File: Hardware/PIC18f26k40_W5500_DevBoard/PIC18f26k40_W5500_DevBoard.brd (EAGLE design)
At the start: 58 x 57 mm, 41 parts, among them J2 MAGJACK, U1 W5500, U2 PIC18F2523-I/SO

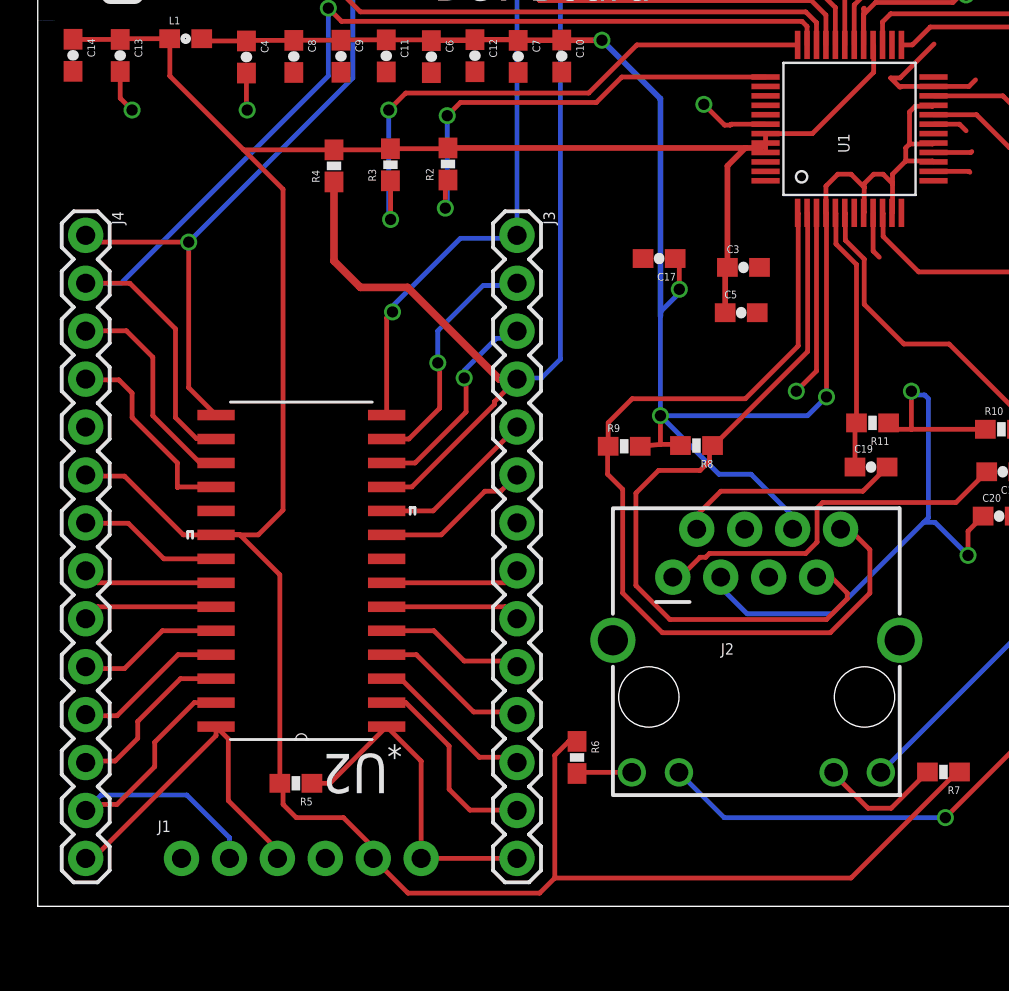
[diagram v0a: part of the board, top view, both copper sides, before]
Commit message: #251 Added more labeling to board
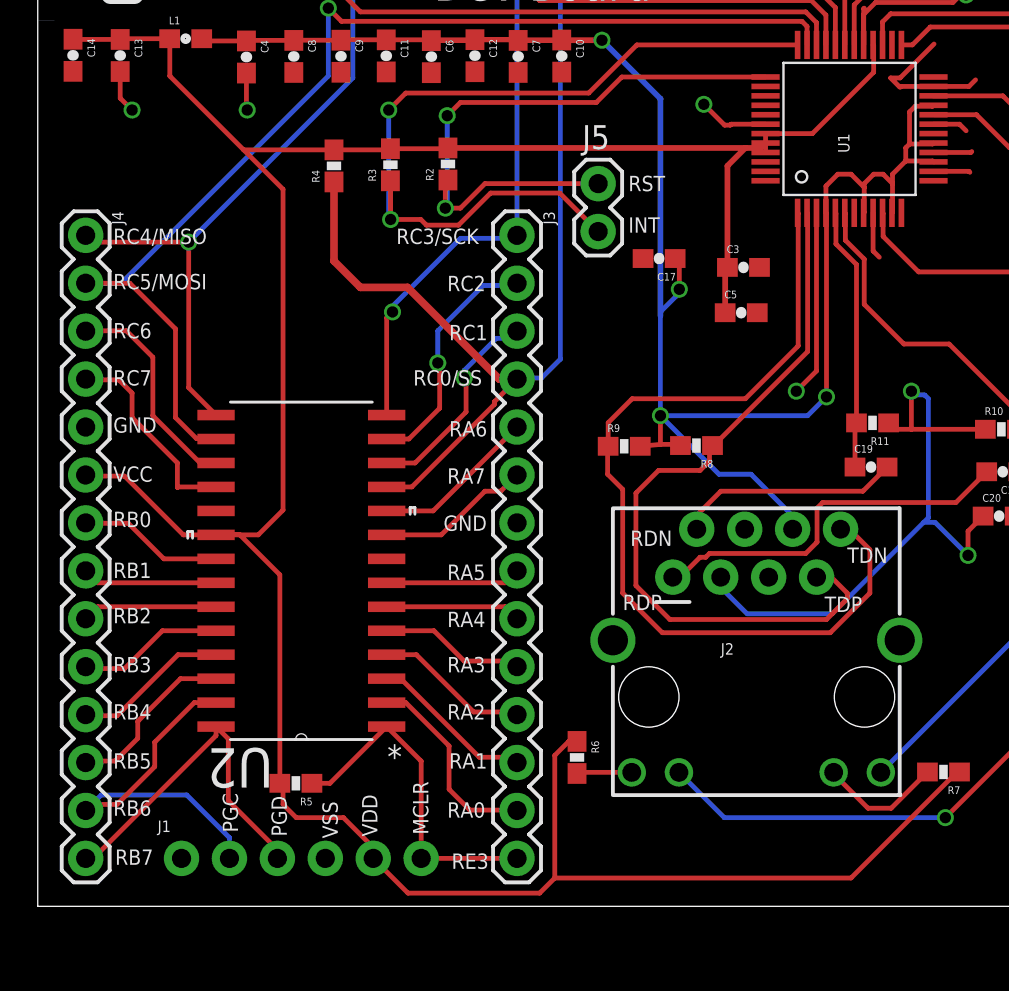
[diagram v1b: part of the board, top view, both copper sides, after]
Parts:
- added J5: (no value), SparkFun-Connectors:1X02
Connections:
- net INT: now also J5.2
- net RST: now also J5.1
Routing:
- net INT: track 31.0 -> 43.7 mm
- net RST: track 24.2 -> 32.8 mm
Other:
- board text added: "GND"
- board text added: "INT"
- board text added: "MCLR"
- board text added: "PGC"
- board text added: "PGD"
- board text added: "RA0"
- board text added: "RA1"
- board text added: "RA2"
- board text added: "RA3"
- board text added: "RA4"
- board text added: "RA5"
- board text added: "RA6"
- board text added: "RA7"
- board text added: "RB0"
- board text added: "RB1"
- board text added: "RB2"
- board text added: "RB3"
- board text added: "RB4"
- board text added: "RB5"
- board text added: "RB6"
- board text added: "RB7"
- board text added: "RC0/SS"
- board text added: "RC1"
- board text added: "RC2"
- board text added: "RC3/SCK"
- board text added: "RC4/MISO"
- board text added: "RC5/MOSI"
- board text added: "RC6"
- board text added: "RC7"
- board text added: "RDN"
- board text added: "RDP"
- board text added: "RE3"
- board text added: "RST"
- board text added: "TDN"
- board text added: "TDP"
- board text added: "VCC"
- board text added: "VDD"
- board text added: "VSS"
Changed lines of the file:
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@@
 <text x="21" y="51" size="1.778" layer="21">W5500</text>
 <text x="21" y="48" size="1.778" layer="21">Dev Board</text>
+<text x="9.8" y="6" size="0.8128" layer="21" rot="R270">PGC</text>
+<text x="13.2" y="3.7" size="0.8128" layer="21" rot="R90">PGD</text>
+<text x="15.9" y="3.6" size="0.8128" layer="21" rot="R90">VSS</text>
+<text x="18" y="3.7" size="0.8128" layer="21" rot="R90">VDD</text>
+<text x="20.7" y="3.8" size="0.8128" layer="21" rot="R90">MCLR</text>
+<text x="23.9" y="2.8" size="0.8128" layer="21" rot="R180">RE3</text>
+<text x="21.7" y="4.7" size="0.8128" layer="21">RA0</text>
+<text x="21.8" y="7.3" size="0.8128" layer="21">RA1</text>
+<text x="21.7" y="9.9" size="0.8128" layer="21">RA2</text>
+<text x="21.7" y="12.4" size="0.8128" layer="21">RA3</text>
+<text x="21.7" y="14.8" size="0.8128" layer="21">RA4</text>
+<text x="21.7" y="17.3" size="0.8128" layer="21">RA5</text>
+<text x="21.5" y="19.9" size="0.8128" layer="21">GND</text>
+<text x="21.7" y="22.4" size="0.8128" layer="21">RA7</text>
+<text x="21.8" y="24.9" size="0.8128" layer="21">RA6</text>
+<text x="19.9" y="27.6" size="0.8128" layer="21">RC0/SS</text>
+<text x="21.8" y="30" size="0.8128" layer="21">RC1</text>
+<text x="21.7" y="32.6" size="0.8128" layer="21">RC2</text>
+<text x="19" y="35.1" size="0.8128" layer="21">RC3/SCK</text>
+<text x="31.3" y="37.9" size="0.8128" layer="21">RST</text>
+<text x="31.3" y="35.7" size="0.8128" layer="21">INT</text>
+<text x="4" y="35.1" size="0.8128" layer="21">RC4/MISO</text>
+<text x="4" y="32.7" size="0.8128" layer="21">RC5/MOSI</text>
+<text x="4" y="30.1" size="0.8128" layer="21">RC6</text>
+<text x="4" y="27.6" size="0.8128" layer="21">RC7</text>
+<text x="4" y="25.1" size="0.8128" layer="21">GND</text>
+<text x="4" y="22.5" size="0.8128" layer="21">VCC</text>
+<text x="4" y="20.1" size="0.8128" layer="21">RB0</text>
+<text x="4" y="17.4" size="0.8128" layer="21">RB1</text>
+<text x="4" y="15" size="0.8128" layer="21">RB2</text>
+<text x="4" y="12.4" size="0.8128" layer="21">RB3</text>
+<text x="4" y="9.9" size="0.8128" layer="21">RB4</text>
+<text x="4" y="7.3" size="0.8128" layer="21">RB5</text>
+<text x="4" y="4.8" size="0.8128" layer="21">RB6</text>
+<text x="4.1" y="2.2" size="0.8128" layer="21">RB7</text>
+<text x="42.9" y="18.2" size="0.8128" layer="21">TDN</text>
+<text x="41.7" y="15.6" size="0.8128" layer="21">TDP</text>
+<text x="31.4" y="19.1" size="0.8128" layer="21">RDN</text>
+<text x="31" y="15.7" size="0.8128" layer="21">RDP</text>
 </plain>
 <attributes>
@@
 <element name="R9" library="SparkFun-Passives" package="0603-RES" value="51" x="31.08" y="24.38"/>
 <element name="U1" library="W5500" package="W5500" value="W5500" x="43.02" y="41.2" rot="R90"/>
-<element name="U2" library="Microchip_By_element14_Batch_1" package="SOIC127P1030X265-28N" value="PIC18F2523-I/SO" x="13.97" y="17.78" rot="R180">
+<element name="U2" library="Microchip_By_element14_Batch_1" package="SOIC127P1030X265-28N" value="PIC18F2523-I/SO" x="13.97" y="17.78" smashed="yes" rot="R180">
 <attribute name="SUPPLIER" value="Microchip" x="13.97" y="17.78" size="1.778" layer="27" rot="R180" display="off"/>
 <attribute name="OC_NEWARK" value="88K5996" x="13.97" y="17.78" size="1.778" layer="27" rot="R180" display="off"/>
@@
 <attribute name="MPN" value="PIC18F2523-I/SO" x="13.97" y="17.78" size="1.778" layer="27" rot="R180" display="off"/>
 <attribute name="OC_FARNELL" value="1332244" x="13.97" y="17.78" size="1.778" layer="27" rot="R180" display="off"/>
+<attribute name="NAME" x="12.4674" y="8.3772" size="2.0828" layer="25" ratio="10" rot="SR180"/>
+<attribute name="VALUE" x="13.2884" y="32.1072" size="2.0828" layer="27" ratio="10" rot="SR270"/>
 </element>
 <element name="Y1" library="SparkFun-Clocks" package="CRYSTAL-SMD-5X3.2-4PAD" value="" x="44.52" y="51.16" rot="R180"/>
 <element name="U$5" library="Heep" package="HEEPLOGOSMALL" value="" x="0" y="47"/>
 <element name="U$6" library="Heep" package="HEEPLETTERS" value="" x="8" y="50"/>
+<element name="J5" library="SparkFun-Connectors" package="1X02" value="" x="29.7" y="38.3" smashed="yes" rot="R270">
+<attribute name="NAME" x="28.8538" y="40.1288" size="1.27" layer="25" ratio="10"/>
+<attribute name="VALUE" x="26.525" y="39.57" size="1.27" layer="27" rot="R270"/>
+</element>
 </elements>
 <signals>
@@
 <wire x1="18.6" y1="36.5" x2="18.7" y2="36.4" width="0.254" layer="16"/>
 <via x="18.7" y="36.4" extent="1-16" drill="0.6" shape="square"/>
-<wire x1="18.7" y1="36.4" x2="18.7" y2="38.44" width="0.254" layer="1"/>
+<wire x1="18.7" y1="38.44" x2="18.7" y2="36.4" width="0.254" layer="1"/>
 <wire x1="18.7" y1="38.44" x2="18.69" y2="38.45" width="0.254" layer="1"/>
+<contactref element="J5" pad="2"/>
+<wire x1="18.7" y1="36.4" x2="20.3" y2="36.4" width="0.254" layer="1"/>
+<wire x1="20.3" y1="36.4" x2="20.6" y2="36.1" width="0.254" layer="1"/>
+<wire x1="20.6" y1="36.1" x2="22.3" y2="36.1" width="0.254" layer="1"/>
+<wire x1="22.3" y1="36.1" x2="24" y2="37.8" width="0.254" layer="1"/>
+<wire x1="24" y1="37.8" x2="27.66" y2="37.8" width="0.254" layer="1"/>
+<wire x1="27.66" y1="37.8" x2="29.7" y2="35.76" width="0.254" layer="1"/>
 </signal>
 <signal name="RST">
@@
 <wire x1="21.7" y1="37.1" x2="21.6" y2="37" width="0.254" layer="16"/>
 <via x="21.6" y="37" extent="1-16" drill="0.6" shape="square"/>
-<wire x1="21.6" y1="37" x2="21.6" y2="38.35" width="0.254" layer="1"/>
+<wire x1="21.6" y1="38.35" x2="21.6" y2="37" width="0.254" layer="1"/>
 <wire x1="21.6" y1="38.35" x2="21.74" y2="38.49" width="0.254" layer="1"/>
+<contactref element="J5" pad="1"/>
+<wire x1="21.6" y1="37" x2="22.4" y2="37" width="0.254" layer="1"/>
+<wire x1="22.4" y1="37" x2="23.7" y2="38.3" width="0.254" layer="1"/>
+<wire x1="23.7" y1="38.3" x2="29.7" y2="38.3" width="0.254" layer="1"/>
 </signal>
 <signal name="VCCA">

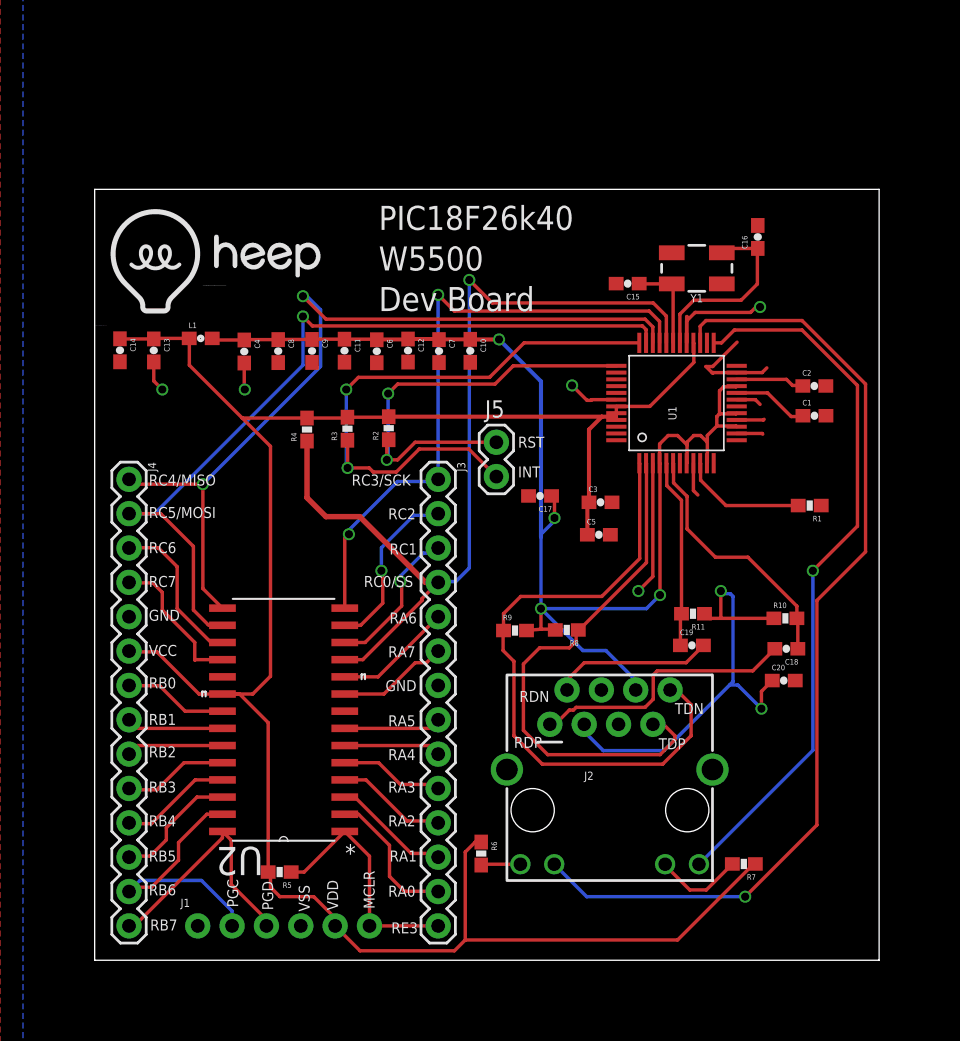
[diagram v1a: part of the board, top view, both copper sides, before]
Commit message: #251 Added room for USB connector and voltage regulator to board
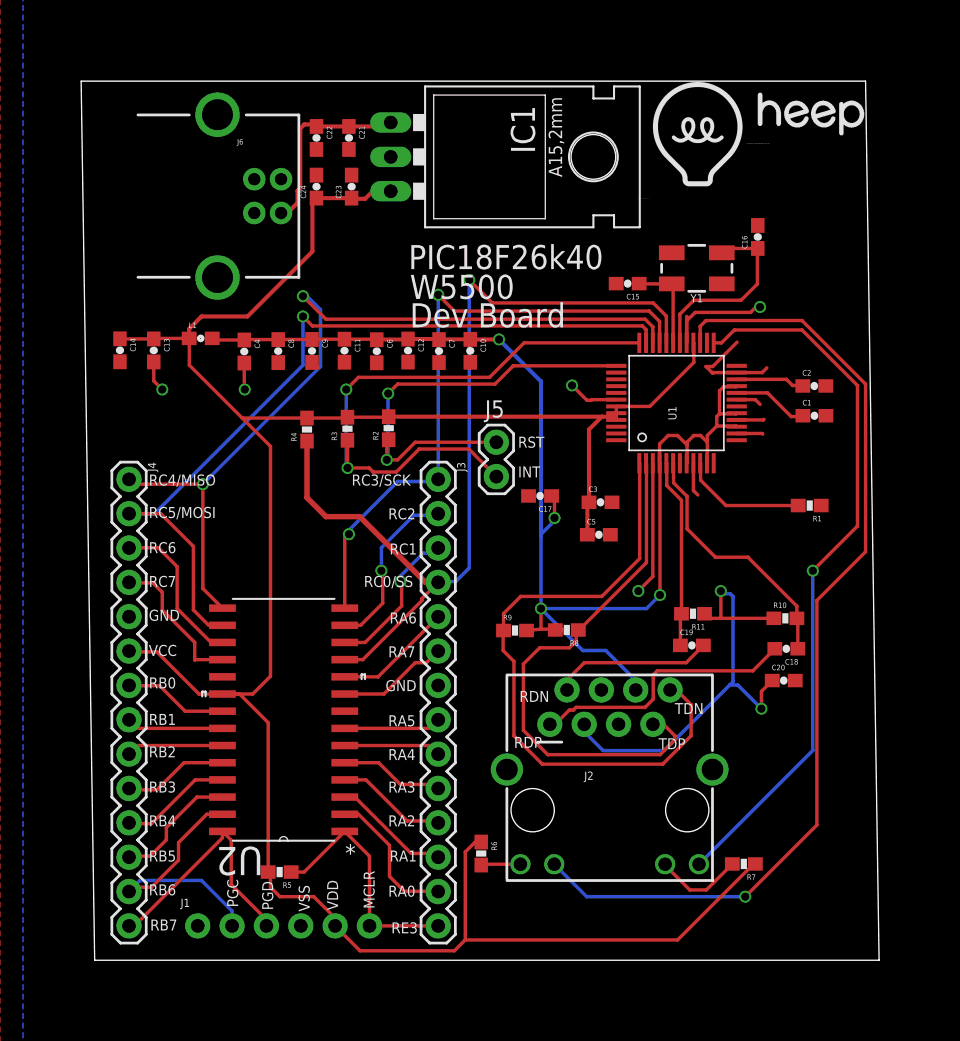
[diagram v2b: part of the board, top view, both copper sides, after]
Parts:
- added C21, C24: 0.1uF, SparkFun-Passives:0603-CAP
- added C22, C23: 10uF, SparkFun-Passives:0603-CAP
- added IC1: (no value), v-reg:78XXL
- added J6: USB-B, SparkFun-Connectors:USB-B-PTH
- moved U$6 41.5 mm to (48.2, 60.5)
- moved U$5 41.2 mm to (40.1, 56.4)
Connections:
- new net 5V: C21.1, C22.1, IC1.IN, J6.VBUS
- net GND: now also C21.2, C22.2, C23.2, C24.2, IC1.GND, J6.GND
- net VCC: now also C23.1, C24.1, IC1.OUT
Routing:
- net VCC: track 156.7 -> 178.7 mm
- net 5V: track 0.00 -> 14.1 mm
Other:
- board size 58 x 57 mm -> 59 x 65 mm
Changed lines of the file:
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@@
 <plain>
 <wire x1="0" y1="0" x2="58" y2="0" width="0" layer="20"/>
-<wire x1="58" y1="0" x2="58" y2="57" width="0" layer="20"/>
-<wire x1="58" y1="57" x2="0" y2="57" width="0" layer="20"/>
-<wire x1="0" y1="57" x2="0" y2="0" width="0" layer="20"/>
-<text x="21" y="54" size="1.778" layer="21">PIC18F26k40</text>
-<text x="21" y="51" size="1.778" layer="21">W5500</text>
-<text x="21" y="48" size="1.778" layer="21">Dev Board</text>
+<wire x1="58" y1="0" x2="57" y2="65" width="0" layer="20"/>
+<wire x1="57" y1="65" x2="-1" y2="65" width="0" layer="20"/>
+<wire x1="-1" y1="65" x2="0" y2="0" width="0" layer="20"/>
+<text x="23.2" y="51.1" size="1.778" layer="21">PIC18F26k40</text>
+<text x="23.3" y="48.9" size="1.778" layer="21">W5500</text>
+<text x="23.3" y="46.8" size="1.778" layer="21">Dev Board</text>
 <text x="9.8" y="6" size="0.8128" layer="21" rot="R270">PGC</text>
 <text x="13.2" y="3.7" size="0.8128" layer="21" rot="R90">PGD</text>
@@
 </element>
 <element name="Y1" library="SparkFun-Clocks" package="CRYSTAL-SMD-5X3.2-4PAD" value="" x="44.52" y="51.16" rot="R180"/>
-<element name="U$5" library="Heep" package="HEEPLOGOSMALL" value="" x="0" y="47"/>
-<element name="U$6" library="Heep" package="HEEPLETTERS" value="" x="8" y="50"/>
+<element name="U$5" library="Heep" package="HEEPLOGOSMALL" value="" x="40.1" y="56.4"/>
+<element name="U$6" library="Heep" package="HEEPLETTERS" value="" x="48.2" y="60.5"/>
 <element name="J5" library="SparkFun-Connectors" package="1X02" value="" x="29.7" y="38.3" smashed="yes" rot="R270">
 <attribute name="NAME" x="28.8538" y="40.1288" size="1.27" layer="25" ratio="10"/>
 <attribute name="VALUE" x="26.525" y="39.57" size="1.27" layer="27" rot="R270"/>
 </element>
+<element name="J6" library="SparkFun-Connectors" package="USB-B-PTH" value="USB-B" x="11.8" y="56.5">
+<attribute name="PROD_ID" value="CONN-08278" x="11.8" y="56.5" size="1.778" layer="27" display="off"/>
+</element>
+<element name="IC1" library="v-reg" package="78XXL" value="" x="25.7" y="59.4" rot="R270"/>
+<element name="C21" library="SparkFun-Passives" package="0603-CAP" value="0.1uF" x="18.8" y="60.8" rot="R270"/>
+<element name="C22" library="SparkFun-Passives" package="0603-CAP" value="10uF" x="16.4" y="60.8" rot="R270"/>
+<element name="C23" library="SparkFun-Passives" package="0603-CAP" value="10uF" x="19" y="57.2" rot="R90"/>
+<element name="C24" library="SparkFun-Passives" package="0603-CAP" value="0.1uF" x="16.4" y="57.2" rot="R90"/>
 </elements>
 <signals>
@@
 <wire x1="44.3" y1="44.2" x2="44.3" y2="45.62" width="0.254" layer="1"/>
 <wire x1="44.3" y1="45.62" x2="44.27" y2="45.65" width="0.254" layer="1"/>
-<wire x1="6.99" y1="45.98" x2="4.41" y2="45.98" width="0.254" layer="1"/>
+<wire x1="4.41" y1="45.98" x2="6.99" y2="45.98" width="0.254" layer="1"/>
 <wire x1="4.41" y1="45.98" x2="4.37" y2="45.94" width="0.254" layer="1"/>
 <wire x1="4.37" y1="45.94" x2="1.88" y2="45.94" width="0.254" layer="1"/>
@@
 <wire x1="13" y1="21" x2="13" y2="38" width="0.254" layer="1"/>
 <wire x1="13" y1="38" x2="10.91" y2="40.09" width="0.254" layer="1"/>
+<contactref element="IC1" pad="OUT"/>
+<contactref element="C23" pad="1"/>
+<contactref element="C24" pad="1"/>
+<wire x1="21.89" y1="56.86" x2="20.56" y2="56.86" width="0.3048" layer="1"/>
+<wire x1="20.56" y1="56.86" x2="20" y2="56.3" width="0.3048" layer="1"/>
+<wire x1="20" y1="56.3" x2="19.05" y2="56.3" width="0.3048" layer="1"/>
+<wire x1="19.05" y1="56.3" x2="19" y2="56.35" width="0.3048" layer="1"/>
+<wire x1="16.4" y1="56.35" x2="19" y2="56.35" width="0.3048" layer="1"/>
+<wire x1="6.99" y1="45.98" x2="6.99" y2="46.69" width="0.3048" layer="1"/>
+<wire x1="6.99" y1="46.69" x2="7.9" y2="47.6" width="0.3048" layer="1"/>
+<wire x1="7.9" y1="47.6" x2="11.3" y2="47.6" width="0.3048" layer="1"/>
+<wire x1="11.3" y1="47.6" x2="16.1" y2="52.4" width="0.3048" layer="1"/>
+<wire x1="16.1" y1="52.4" x2="16.1" y2="56.05" width="0.3048" layer="1"/>
+<wire x1="16.1" y1="56.05" x2="16.4" y2="56.35" width="0.3048" layer="1"/>
 </signal>
 <signal name="GND">
@@
 <wire x1="11.06" y1="42.24" x2="11.1" y2="42.2" width="0.254" layer="1"/>
 <via x="11.1" y="42.2" extent="1-16" drill="0.6" shape="square"/>
+<contactref element="J6" pad="GND"/>
+<contactref element="IC1" pad="GND"/>
+<contactref element="C24" pad="2"/>
+<contactref element="C23" pad="2"/>
+<contactref element="C21" pad="2"/>
+<contactref element="C22" pad="2"/>
 </signal>
 <signal name="N$1">
@@
 <wire x1="2.62" y1="7.7" x2="2.54" y2="7.62" width="0.254" layer="1"/>
 </signal>
+<signal name="5V">
+<contactref element="J6" pad="VBUS"/>
+<contactref element="IC1" pad="IN"/>
+<contactref element="C22" pad="1"/>
+<contactref element="C21" pad="1"/>
+<wire x1="13.7812" y1="55.25" x2="14.25" y2="55.25" width="0.3048" layer="1"/>
+<wire x1="14.25" y1="55.25" x2="15" y2="56" width="0.3048" layer="1"/>
+<wire x1="15" y1="56" x2="15" y2="56.9" width="0.3048" layer="1"/>
+<wire x1="15" y1="56.9" x2="15.2" y2="57.1" width="0.3048" layer="1"/>
+<wire x1="15.2" y1="57.1" x2="15.2" y2="61.5" width="0.3048" layer="1"/>
+<wire x1="15.2" y1="61.5" x2="15.5" y2="61.8" width="0.3048" layer="1"/>
+<wire x1="15.5" y1="61.8" x2="16.25" y2="61.8" width="0.3048" layer="1"/>
+<wire x1="16.25" y1="61.8" x2="16.4" y2="61.65" width="0.3048" layer="1"/>
+<wire x1="16.4" y1="61.65" x2="18.8" y2="61.65" width="0.3048" layer="1"/>
+<wire x1="18.8" y1="61.65" x2="21.6" y2="61.65" width="0.3048" layer="1"/>
+<wire x1="21.6" y1="61.65" x2="21.89" y2="61.94" width="0.3048" layer="1"/>
+</signal>
 </signals>
